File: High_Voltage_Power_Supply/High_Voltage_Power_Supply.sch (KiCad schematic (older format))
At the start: 100 parts, among them J1 Conn_01x02_Female, J2 Conn_01x02_Female, J3 Conn_01x02_Female, J4 Conn_01x12_Female, Q1 Q_NMOS_GDS, Q2 Q_NMOS_GDS, Q3 Q_NMOS_GDS, Q4 Q_NIGBT_GCE, U1 LT3751-TSSOP, U10 ADR3412, U11 LMR16030S, U2 LT3751-TSSOP, U3 ZXGD3004E6, U4 ZXGD3004E6, U5 MC14504B, U6 MC14504B, U7 LM7805, U8 LM7805, U9 LMV331

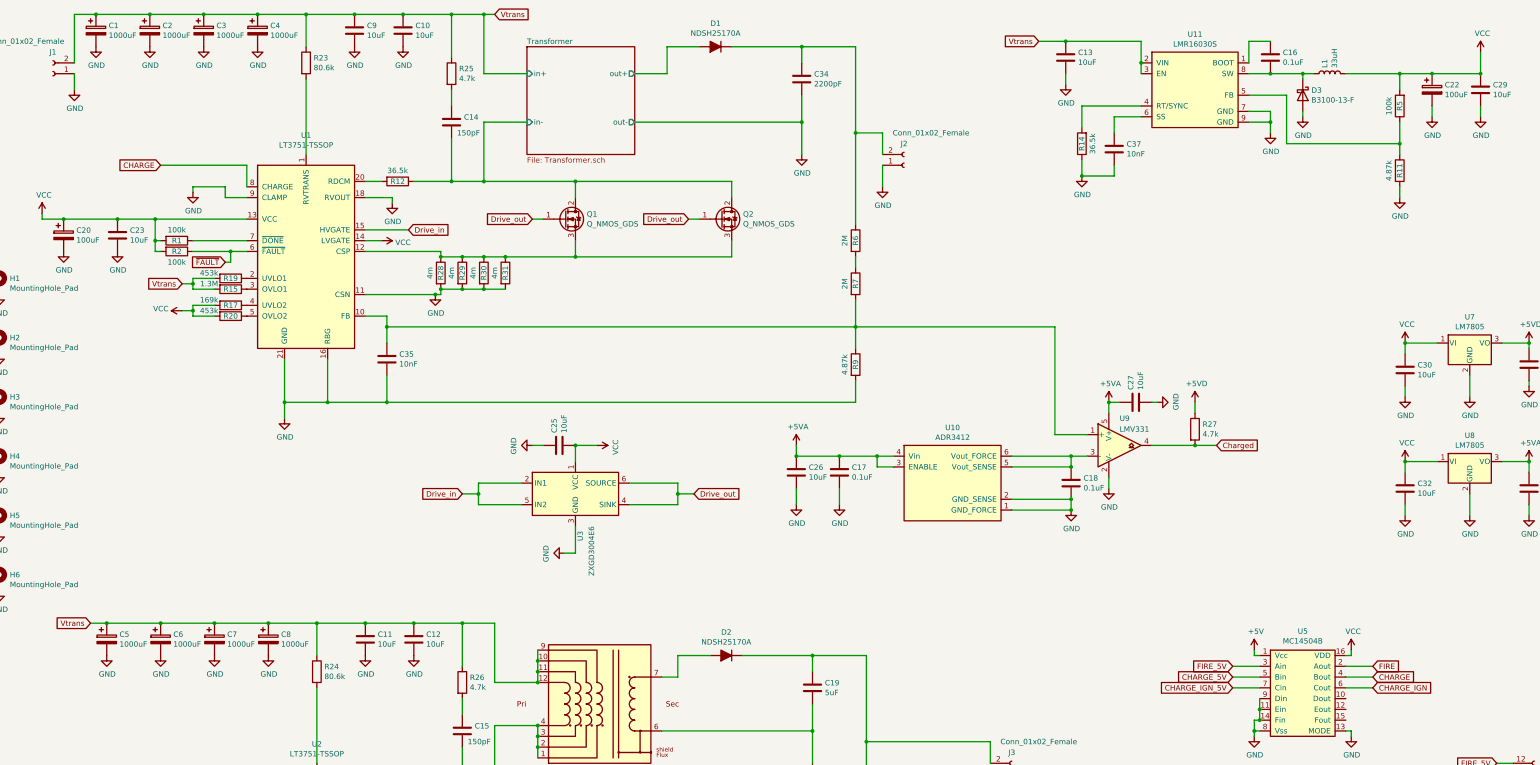
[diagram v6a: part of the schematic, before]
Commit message: Edited schematic to use new buck converter chip.
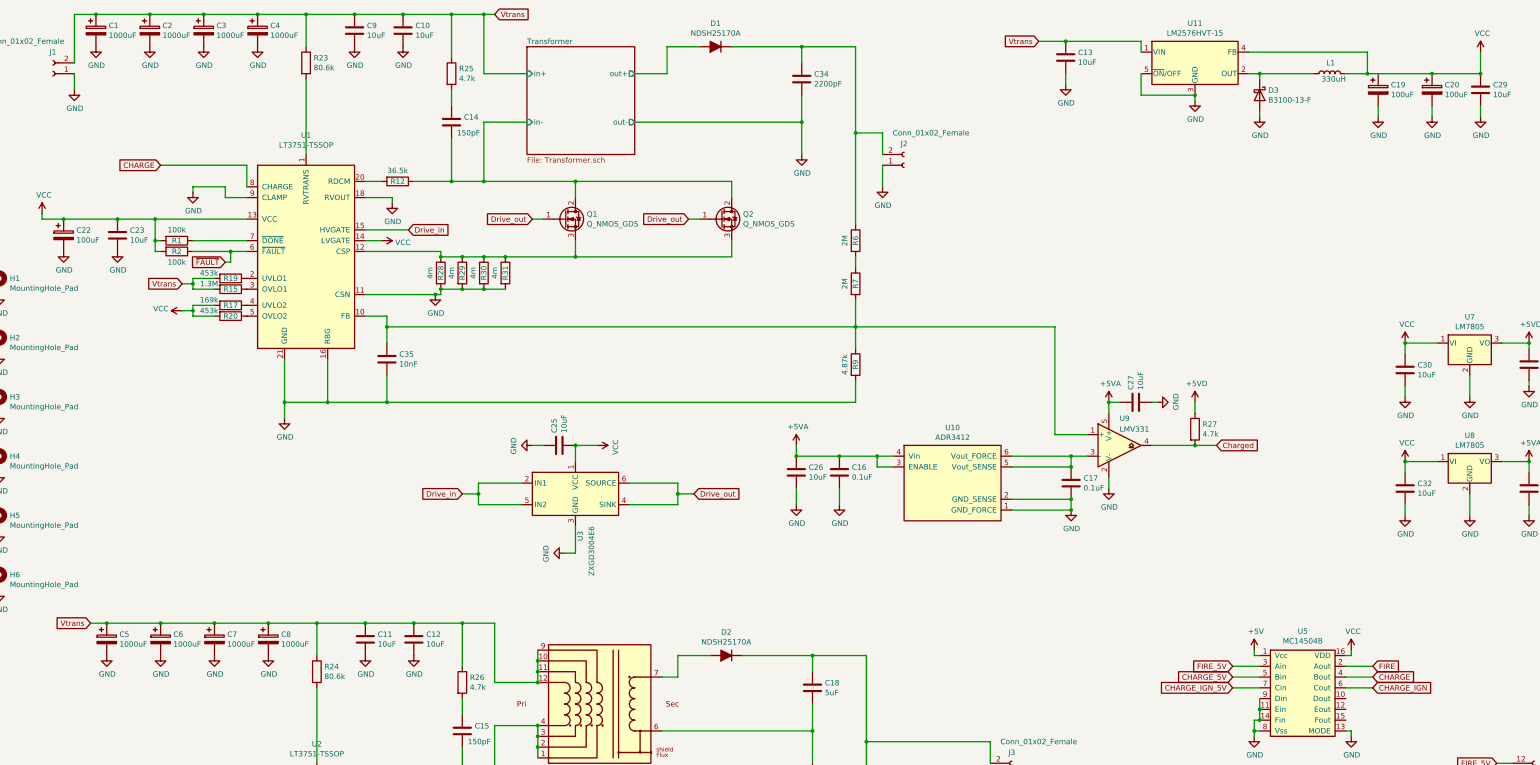
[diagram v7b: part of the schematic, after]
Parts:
- removed C16: 0.1uF, Capacitor_SMD:C_1206_3216Metric, symbol Device:C
- removed C37: 10nF, Capacitor_SMD:C_0603_1608Metric, symbol Device:C
- removed R11: 4.87k, Resistor_SMD:R_1206_3216Metric, symbol Device:R
- removed R14: 36.5k, Resistor_SMD:R_0603_1608Metric, symbol Device:R
- removed R5: 100k, Resistor_SMD:R_0603_1608Metric, symbol Device:R
- removed U11: LMR16030S, Package_SO:SOIC-8-1EP_3.9x4.9mm_P1.27mm_EP2.41x3.3mm_ThermalVias, symbol High_Voltage_Power_Supply:LMR16030S
- added C19: 100uF, Capacitor_THT:CP_Radial_D8.0mm_P5.00mm, symbol Device:CP
- added U11: LM2576HVT-15, Package_TO_SOT_THT:TO-220-5_Vertical, symbol Regulator_Switching:LM2576HVT-15
- L1: value 33uH -> 330uH; footprint Inductor_SMD:L_Bourns_SRR1260 -> High_Voltage_Power_Supply:60B334C; Link https://www.digikey.com/en/products/detail/bourns-inc/SRR12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 -> https://www.digikey.com/en/products/detail/60B334C/811-2464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
- renumbered C17 to C16, C18 to C17, C19 to C18, C22 to C20, C20 to C22
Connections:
- net GND: now also C19.2, U11.3 (GND), U11.5 (~ON~/OFF)
- net VCC: now also U11.4 (FB)
- net Vtrans: now also U11.1 (VIN)
- net at D3.1 (K), L1.1: now also U11.2 (OUT)
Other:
- moved on the sheet: D3

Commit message: Rough component placements to allow heat sinks to be installed
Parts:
- H5, H6: footprint MountingHole:MountingHole_3.2mm_M3_Pad_Via -> MountingHole:MountingHole_3.2mm_M3; symbol Mechanical:MountingHole_Pad -> Mechanical:MountingHole
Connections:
- net GND: no longer H5.1, H6.1
- net VCC: now also C19.1
- net ~FAULT_5V~: now also J4.8 (Pin_8); no longer J4.9 (Pin_9)
- net ~FAULT_IGN_5V~: now also J4.9 (Pin_9); no longer J4.8 (Pin_8)
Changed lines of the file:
@@
 	4200 3650 4400 3650
-$Comp
-L High_Voltage_Power_Supply:LT3751-TSSOP U1
-U 1 1 5B89BF58
-P 3650 3150
-F 0 "U1" H 3650 4328 50  0000 C CNN
-F 1 "LT3751-TSSOP" H 3650 4237 50  0000 C CNN
-F 2 "Package_SO:HTSSOP-20-1EP_4.4x6.5mm_P0.65mm_EP3.4x6.5mm_ThermalVias" H 3650 3150 50  0001 C CNN
-F 3 "http://www.linear.com/docs/27024" H 3650 3150 50  0001 C CNN
-F 4 "Want LT3751I if possible as it goes down to -40c, but LT3751E works if needed (only to 0c)" H 3650 3150 50  0001 C CNN "Note"
-F 5 "https://www.digikey.com/product-detail/en/analog-devices-inc/LT3751EFE-TRPBF/LT3751EFE-TRPBFCT-ND/8040620" H 3650 3150 50  0001 C CNN "Link (LT3751E)"
-	1    3650 3150
-	1    0    0    -1
-$EndComp
 $Comp
 L Device:R R12
@@
 	1    0    0    -1
 $EndComp
-Wire Wire Line
-	1200 2750 1400 2750
 $Comp
 L Device:CP C22
@@
 	1    0    0    -1
 $EndComp
-Text GLabel 14300 8200 0    50   Input ~ 0
+Text GLabel 14750 8100 0    50   Input ~ 0
 ~FAULT_IGN_5V~
-Wire Wire Line
-	14850 8200 14300 8200
-Text GLabel 14750 8100 0    50   Input ~ 0
+Text GLabel 14150 8200 0    50   Input ~ 0
 ~FAULT_5V~
 Wire Wire Line
 	14750 8100 14850 8100
-Wire Wire Line
-	14850 8000 14300 8000
 Wire Wire Line
 	14850 7900 14700 7900
@@
 Wire Wire Line
 	10100 8450 10100 8550
-Text GLabel 14300 8000 0    50   Input ~ 0
+Text GLabel 14100 8000 0    50   Input ~ 0
 CHARGE_IGN_5V
 Text GLabel 14700 7900 0    50   Input ~ 0
@@
 $EndComp
 $Comp
-L Mechanical:MountingHole_Pad H5
+L Mechanical:MountingHole H5
 U 1 1 608F41BF
 P 800 5550
 F 0 "H5" H 900 5599 50  0000 L CNN
 F 1 "MountingHole_Pad" H 900 5508 50  0000 L CNN
-F 2 "MountingHole:MountingHole_3.2mm_M3_Pad_Via" H 800 5550 50  0001 C CNN
+F 2 "MountingHole:MountingHole_3.2mm_M3" H 800 5550 50  0001 C CNN
 F 3 "~" H 800 5550 50  0001 C CNN
 	1    800  5550
@@
 $EndComp
 $Comp
-L power:GND #PWR0181
-U 1 1 608F41C5
-P 800 5650
-F 0 "#PWR0181" H 800 5400 50  0001 C CNN
-F 1 "GND" H 805 5477 50  0000 C CNN
-F 2 "" H 800 5650 50  0001 C CNN
-F 3 "" H 800 5650 50  0001 C CNN
-	1    800  5650
-	1    0    0    -1
-$EndComp
-$Comp
-L Mechanical:MountingHole_Pad H6
+L Mechanical:MountingHole H6
 U 1 1 60914351
 P 800 6100
 F 0 "H6" H 900 6149 50  0000 L CNN
 F 1 "MountingHole_Pad" H 900 6058 50  0000 L CNN
-F 2 "MountingHole:MountingHole_3.2mm_M3_Pad_Via" H 800 6100 50  0001 C CNN
+F 2 "MountingHole:MountingHole_3.2mm_M3" H 800 6100 50  0001 C CNN
 F 3 "~" H 800 6100 50  0001 C CNN
 	1    800  6100
-	1    0    0    -1
-$EndComp
-$Comp
-L power:GND #PWR0182
-U 1 1 60914357
-P 800 6200
-F 0 "#PWR0182" H 800 5950 50  0001 C CNN
-F 1 "GND" H 805 6027 50  0000 C CNN
-F 2 "" H 800 6200 50  0001 C CNN
-F 3 "" H 800 6200 50  0001 C CNN
-	1    800  6200
 	1    0    0    -1
 $EndComp
@@
 Connection ~ 13500 1400
 Wire Wire Line
-	13500 1400 14100 1400
+	13500 1400 13600 1400
 Connection ~ 12500 1400
 Wire Wire Line
@@
 Wire Wire Line
 	13600 1800 13600 1700
+Connection ~ 13600 1400
+Wire Wire Line
+	13600 1400 14100 1400
+Wire Wire Line
+	1200 2750 1400 2750
+$Comp
+L High_Voltage_Power_Supply:LT3751-TSSOP U1
+U 1 1 5B89BF58
+P 3650 3150
+F 0 "U1" H 3650 4328 50  0000 C CNN
+F 1 "LT3751-TSSOP" H 3650 4237 50  0000 C CNN
+F 2 "Package_SO:HTSSOP-20-1EP_4.4x6.5mm_P0.65mm_EP3.4x6.5mm_ThermalVias" H 3650 3150 50  0001 C CNN
+F 3 "http://www.linear.com/docs/27024" H 3650 3150 50  0001 C CNN
+F 4 "Want LT3751I if possible as it goes down to -40c, but LT3751E works if needed (only to 0c)" H 3650 3150 50  0001 C CNN "Note"
+F 5 "https://www.digikey.com/product-detail/en/analog-devices-inc/LT3751EFE-TRPBF/LT3751EFE-TRPBFCT-ND/8040620" H 3650 3150 50  0001 C CNN "Link (LT3751E)"
+	1    3650 3150
+	1    0    0    -1
+$EndComp
+Wire Wire Line
+	14100 8000 14850 8000
+Wire Wire Line
+	14150 8200 14850 8200
 $EndSCHEMATC
